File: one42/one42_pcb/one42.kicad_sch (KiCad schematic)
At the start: 37 parts, among them J1 Conn_01x04_Female, Q1 AO3401A, SW44 SW_SPDT, U1 TP4054, U2 AP2112K-3.3, U3 nRF52840_holyiot_18010, U4 One42

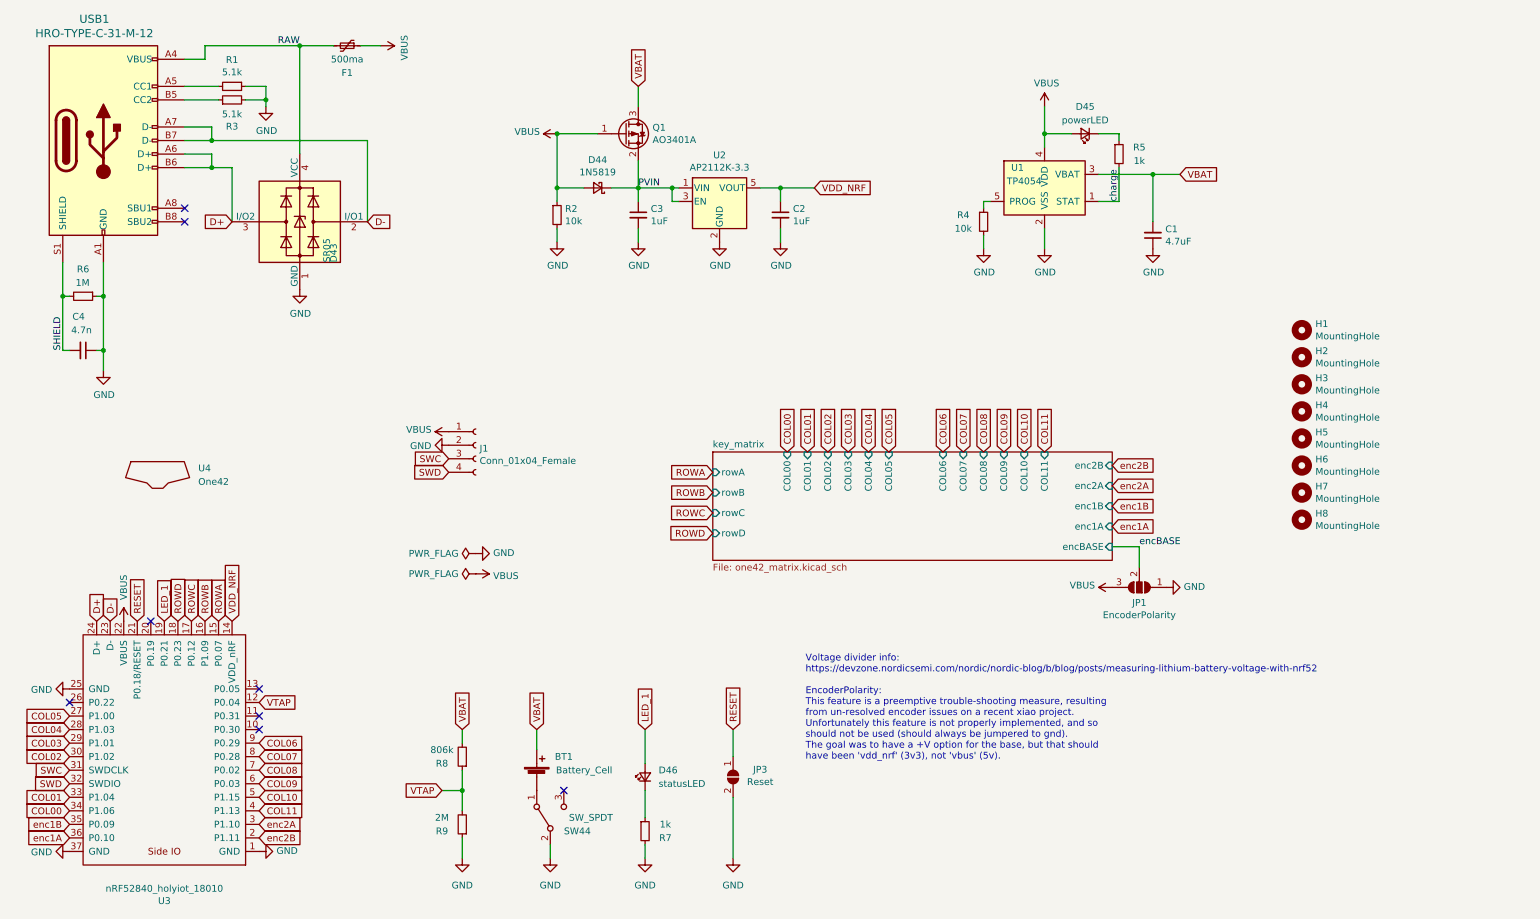
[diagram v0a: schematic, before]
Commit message: [one42] version 1.0
- Relocated corner-thumb switch diodes
- Removed encoder base-supply option
- Fixed 'R5' silkscreen
- Fixed programmer-header V+ to 3v3
- Moved power sw. inboard
- Mounting holes routed to ground
- Battery-pad size reduced
- Relocated power-routing/switching components
- Repositioned 'XLII' text
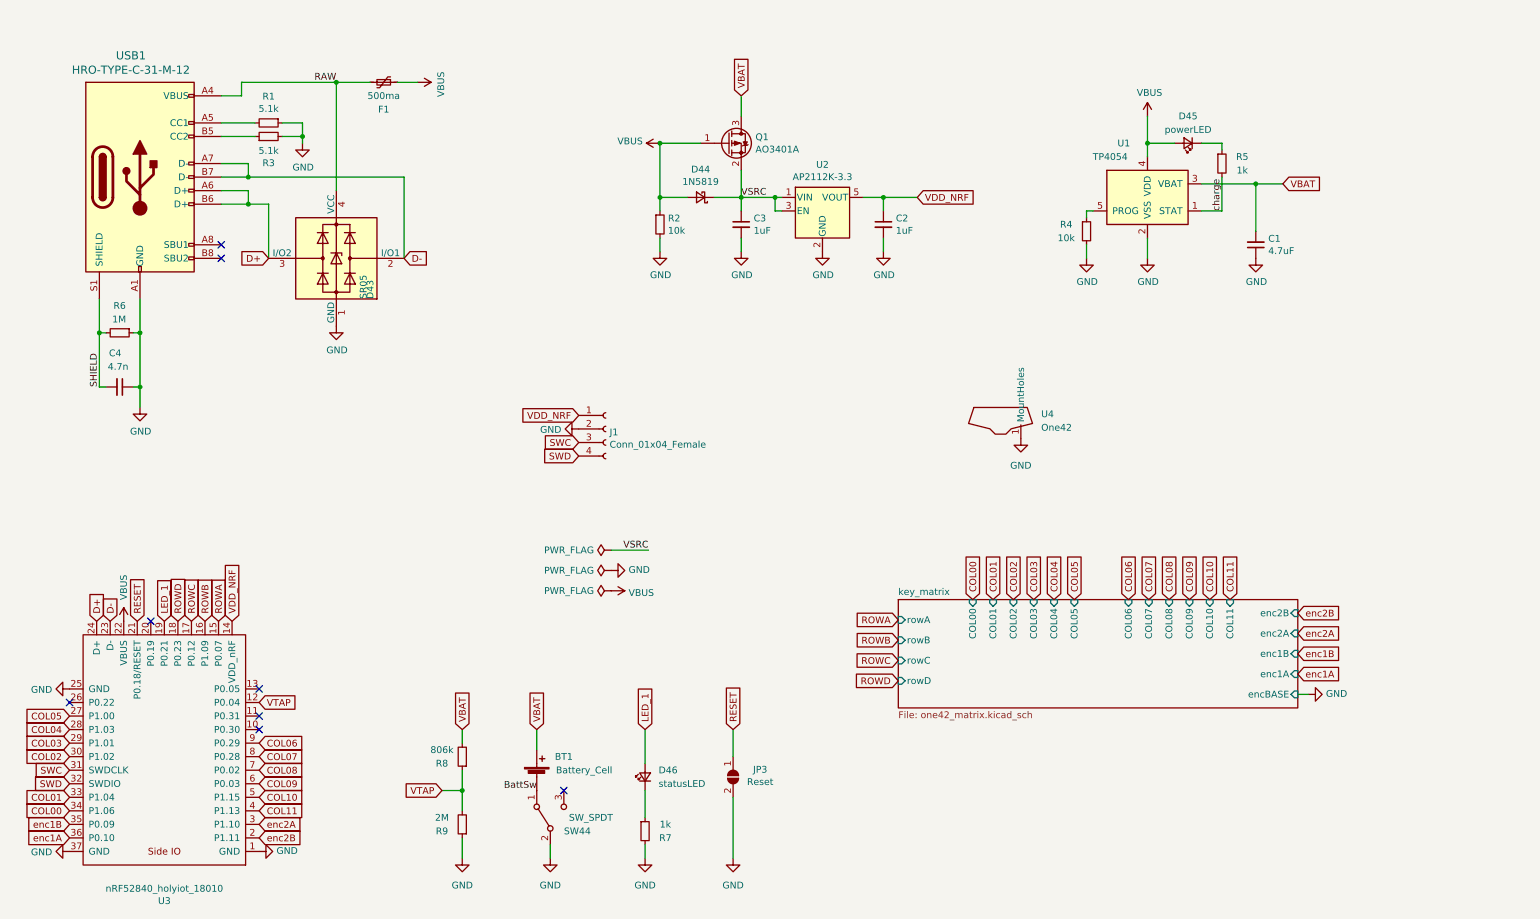
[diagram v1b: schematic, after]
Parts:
- removed H1, H2, H3, H4, H5, H6, H7, H8: MountingHole, MountingHole:MountingHole_2.2mm_M2_Pad, symbol Mechanical:MountingHole
- removed JP1: EncoderPolarity, Jumper:SolderJumper-3_P1.3mm_Open_RoundedPad1.0x1.5mm, symbol Jumper:SolderJumper_3_Open
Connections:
- net GND: now also U4.1 (MountHoles)
- net VBUS: no longer J1.1 (Pin_1)
- net VDD_NRF: now also J1.1 (Pin_1)
- net BattSw: now reaches BT1.2 (-), SW44.1 (A)
- net PVIN renamed VSRC
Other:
- note removed: "Voltage divider info: https://devzone.nordicsemi.com/nordic/nordic-blog/b/blog/posts/measuring-lithium-battery-voltage-with-nrf52 EncoderPolarity: This feature is a preemptive trouble-shooting measure, resulting from un-resolved encoder issues on a recent xiao project. Unfortunately this feature is not properly implemented, and so should not be used (should always be jumpered to gnd). The goal wa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"
- moved on the sheet: C1, C2, C3, C4, D43, D44, D45, F1, J1, Q1, R1, R2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
